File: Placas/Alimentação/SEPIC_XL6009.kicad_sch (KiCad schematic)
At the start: 11 parts, among them U3 XL6009

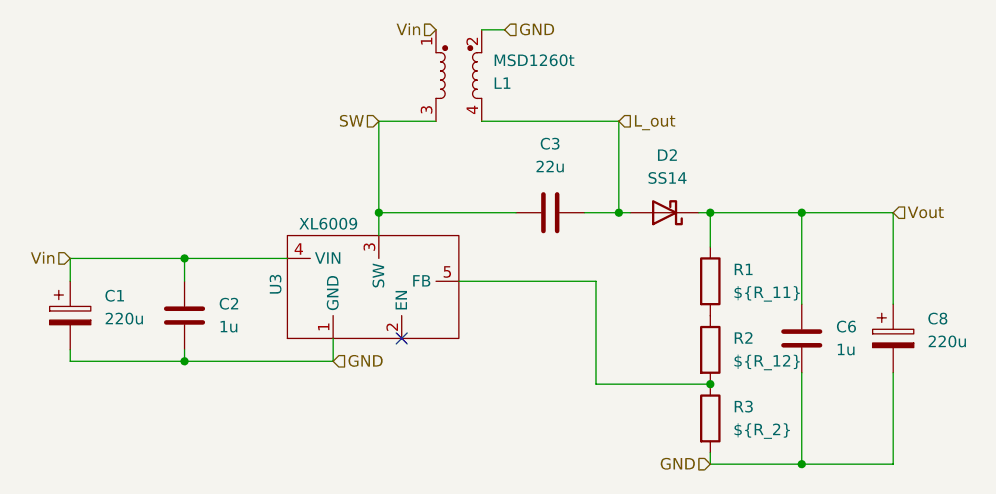
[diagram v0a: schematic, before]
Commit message: Criação dos arquivos em C para o firmware dos dois micros e script em python para salvar aquisição dos dados e envio de comandos
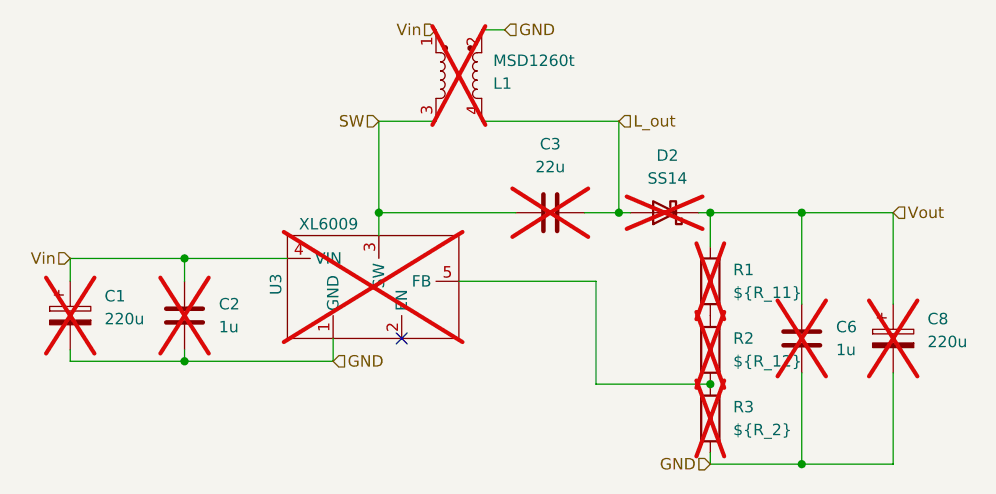
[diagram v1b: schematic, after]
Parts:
- C1, C2, C3, C6, C8, D2, L1, R1, R2, R3, U3: now not fitted
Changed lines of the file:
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@@
 		(in_bom yes)
 		(on_board yes)
-		(dnp no)
+		(dnp yes)
 		(fields_autoplaced yes)
 		(property "Reference" "C6"
@@
 				(path "/a66ab151-18e3-44fa-8b10-f32a50ff2a79/a16597ec-0be9-4bb9-86cc-8ed7be0e884a/6dbd06f9-0043-4804-b698-8f4038b025b3"
 					(reference "C6")
-					(unit 1)
-				)
-				(path "/a66ab151-18e3-44fa-8b10-f32a50ff2a79/d0bed551-f4e5-4843-95bd-8307d1ffe43d/7e52b7f8-3529-4982-b0df-bdd06b8e16ba"
-					(reference "C17")
 					(unit 1)
 				)
@@
 		(in_bom yes)
 		(on_board yes)
-		(dnp no)
+		(dnp yes)
 		(property "Reference" "L1"
 			(at 138.43 80.8991 90)
@@
 					(unit 1)
 				)
-				(path "/a66ab151-18e3-44fa-8b10-f32a50ff2a79/d0bed551-f4e5-4843-95bd-8307d1ffe43d/7e52b7f8-3529-4982-b0df-bdd06b8e16ba"
-					(reference "L4")
-					(unit 1)
-				)
 				(path "/a66ab151-18e3-44fa-8b10-f32a50ff2a79/f52dd514-ccdf-4a34-8316-0d66dec1a789/5f40724c-2ef8-45e6-9dce-f12c833737b3"
 					(reference "L3")
@@
 		(in_bom yes)
 		(on_board yes)
-		(dnp no)
+		(dnp yes)
 		(fields_autoplaced yes)
 		(property "Reference" "R2"
@@
 					(unit 1)
 				)
-				(path "/a66ab151-18e3-44fa-8b10-f32a50ff2a79/d0bed551-f4e5-4843-95bd-8307d1ffe43d/7e52b7f8-3529-4982-b0df-bdd06b8e16ba"
-					(reference "R8")
-					(unit 1)
-				)
 				(path "/a66ab151-18e3-44fa-8b10-f32a50ff2a79/f52dd514-ccdf-4a34-8316-0d66dec1a789/5f40724c-2ef8-45e6-9dce-f12c833737b3"
 					(reference "R5")
@@
 		(in_bom yes)
 		(on_board yes)
-		(dnp no)
+		(dnp yes)
 		(fields_autoplaced yes)
 		(property "Reference" "R1"
@@
 					(unit 1)
 				)
-				(path "/a66ab151-18e3-44fa-8b10-f32a50ff2a79/d0bed551-f4e5-4843-95bd-8307d1ffe43d/7e52b7f8-3529-4982-b0df-bdd06b8e16ba"
-					(reference "R7")
-					(unit 1)
-				)
 				(path "/a66ab151-18e3-44fa-8b10-f32a50ff2a79/f52dd514-ccdf-4a34-8316-0d66dec1a789/5f40724c-2ef8-45e6-9dce-f12c833737b3"
 					(reference "R4")
@@
 		(in_bom yes)
 		(on_board yes)
-		(dnp no)
+		(dnp yes)
 		(fields_autoplaced yes)
 		(property "Reference" "C1"
@@
 					(unit 1)
 				)
-				(path "/a66ab151-18e3-44fa-8b10-f32a50ff2a79/d0bed551-f4e5-4843-95bd-8307d1ffe43d/7e52b7f8-3529-4982-b0df-bdd06b8e16ba"
-					(reference "C14")
-					(unit 1)
-				)
 				(path "/a66ab151-18e3-44fa-8b10-f32a50ff2a79/f52dd514-ccdf-4a34-8316-0d66dec1a789/5f40724c-2ef8-45e6-9dce-f12c833737b3"
 					(reference "C9")
@@
 		(in_bom yes)
 		(on_board yes)
-		(dnp no)
+		(dnp yes)
 		(property "Reference" "U3"
 			(at 114.3 104.394 0)
@@
 					(unit 1)
 				)
-				(path "/a66ab151-18e3-44fa-8b10-f32a50ff2a79/d0bed551-f4e5-4843-95bd-8307d1ffe43d/7e52b7f8-3529-4982-b0df-bdd06b8e16ba"
-					(reference "U5")
-					(unit 1)
-				)
 				(path "/a66ab151-18e3-44fa-8b10-f32a50ff2a79/f52dd514-ccdf-4a34-8316-0d66dec1a789/5f40724c-2ef8-45e6-9dce-f12c833737b3"
 					(reference "U4")
@@
 		(in_bom yes)
 		(on_board yes)
-		(dnp no)
+		(dnp yes)
 		(fields_autoplaced yes)
 		(property "Reference" "D2"
@@
 					(unit 1)
 				)
-				(path "/a66ab151-18e3-44fa-8b10-f32a50ff2a79/d0bed551-f4e5-4843-95bd-8307d1ffe43d/7e52b7f8-3529-4982-b0df-bdd06b8e16ba"
-					(reference "D4")
-					(unit 1)
-				)
 				(path "/a66ab151-18e3-44fa-8b10-f32a50ff2a79/f52dd514-ccdf-4a34-8316-0d66dec1a789/5f40724c-2ef8-45e6-9dce-f12c833737b3"
 					(reference "D3")
@@
 		(in_bom yes)
 		(on_board yes)
-		(dnp no)
+		(dnp yes)
 		(fields_autoplaced yes)
 		(property "Reference" "C8"
@@
 					(unit 1)
 				)
-				(path "/a66ab151-18e3-44fa-8b10-f32a50ff2a79/d0bed551-f4e5-4843-95bd-8307d1ffe43d/7e52b7f8-3529-4982-b0df-bdd06b8e16ba"
-					(reference "C18")
-					(unit 1)
-				)
 				(path "/a66ab151-18e3-44fa-8b10-f32a50ff2a79/f52dd514-ccdf-4a34-8316-0d66dec1a789/5f40724c-2ef8-45e6-9dce-f12c833737b3"
 					(reference "C13")
@@
 		(in_bom yes)
 		(on_board yes)
-		(dnp no)
+		(dnp yes)
 		(fields_autoplaced yes)
 		(property "Reference" "C3"
@@
 					(unit 1)
 				)
-				(path "/a66ab151-18e3-44fa-8b10-f32a50ff2a79/d0bed551-f4e5-4843-95bd-8307d1ffe43d/7e52b7f8-3529-4982-b0df-bdd06b8e16ba"
-					(reference "C16")
-					(unit 1)
-				)
 				(path "/a66ab151-18e3-44fa-8b10-f32a50ff2a79/f52dd514-ccdf-4a34-8316-0d66dec1a789/5f40724c-2ef8-45e6-9dce-f12c833737b3"
 					(reference "C11")
@@
 		(in_bom yes)
 		(on_board yes)
-		(dnp no)
+		(dnp yes)
 		(fields_autoplaced yes)
 		(property "Reference" "C2"
@@
 					(unit 1)
 				)
-				(path "/a66ab151-18e3-44fa-8b10-f32a50ff2a79/d0bed551-f4e5-4843-95bd-8307d1ffe43d/7e52b7f8-3529-4982-b0df-bdd06b8e16ba"
-					(reference "C15")
-					(unit 1)
-				)
 				(path "/a66ab151-18e3-44fa-8b10-f32a50ff2a79/f52dd514-ccdf-4a34-8316-0d66dec1a789/5f40724c-2ef8-45e6-9dce-f12c833737b3"
 					(reference "C10")
@@
 		(in_bom yes)
 		(on_board yes)
-		(dnp no)
+		(dnp yes)
 		(fields_autoplaced yes)
 		(property "Reference" "R3"
@@
 					(unit 1)
 				)
-				(path "/a66ab151-18e3-44fa-8b10-f32a50ff2a79/d0bed551-f4e5-4843-95bd-8307d1ffe43d/7e52b7f8-3529-4982-b0df-bdd06b8e16ba"
-					(reference "R9")
-					(unit 1)
-				)
